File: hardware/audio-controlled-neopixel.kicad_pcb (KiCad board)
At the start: 2 copper layers, 96 x 56 mm, 63 parts, among them J1 AudioJack3_Ground, J2 AudioJack3_Ground, J3 KF2EDGK, J4 KF2EDGK, J5 KF2EDGK, J6 Conn_01x01_Female, J7 Conn_01x01_Female, J8 Conn_01x01_Female, J9 Conn_01x01_Female, SW1 SW_SPST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

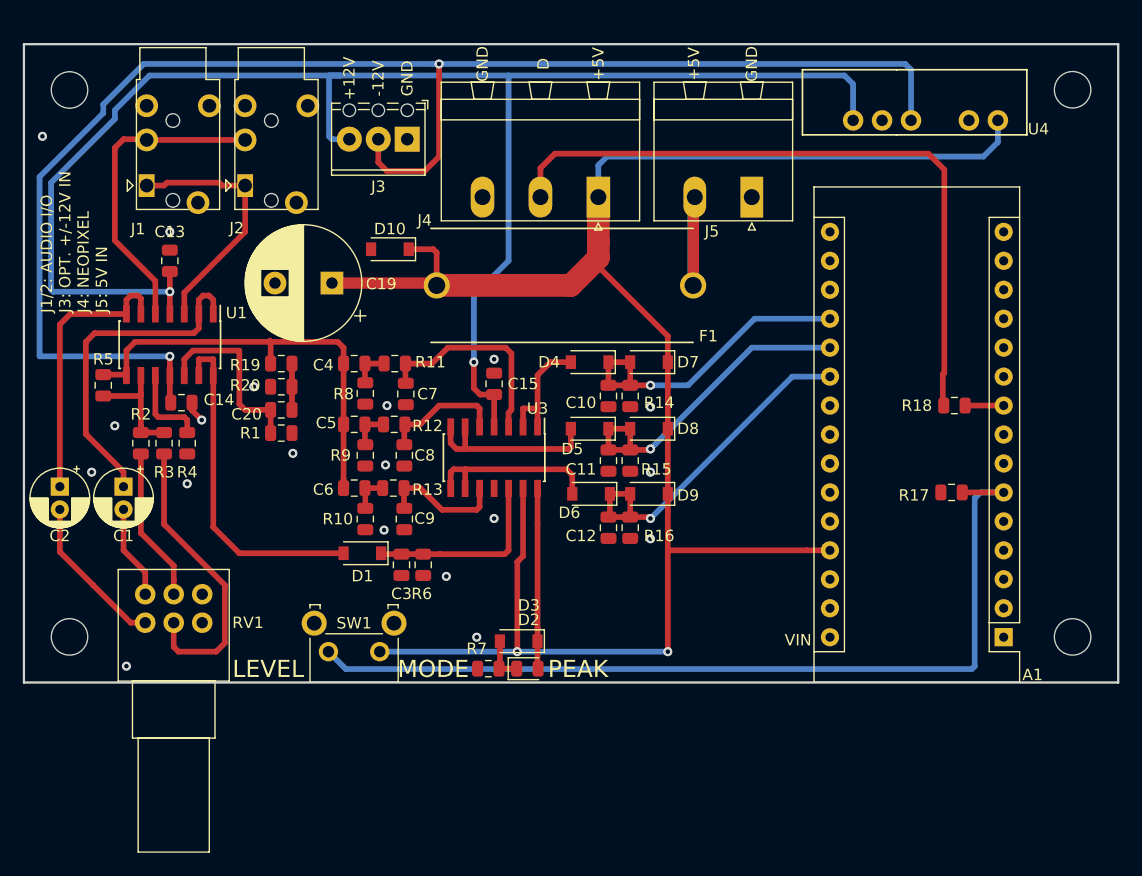
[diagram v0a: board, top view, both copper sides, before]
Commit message: updated some footprints and symbols
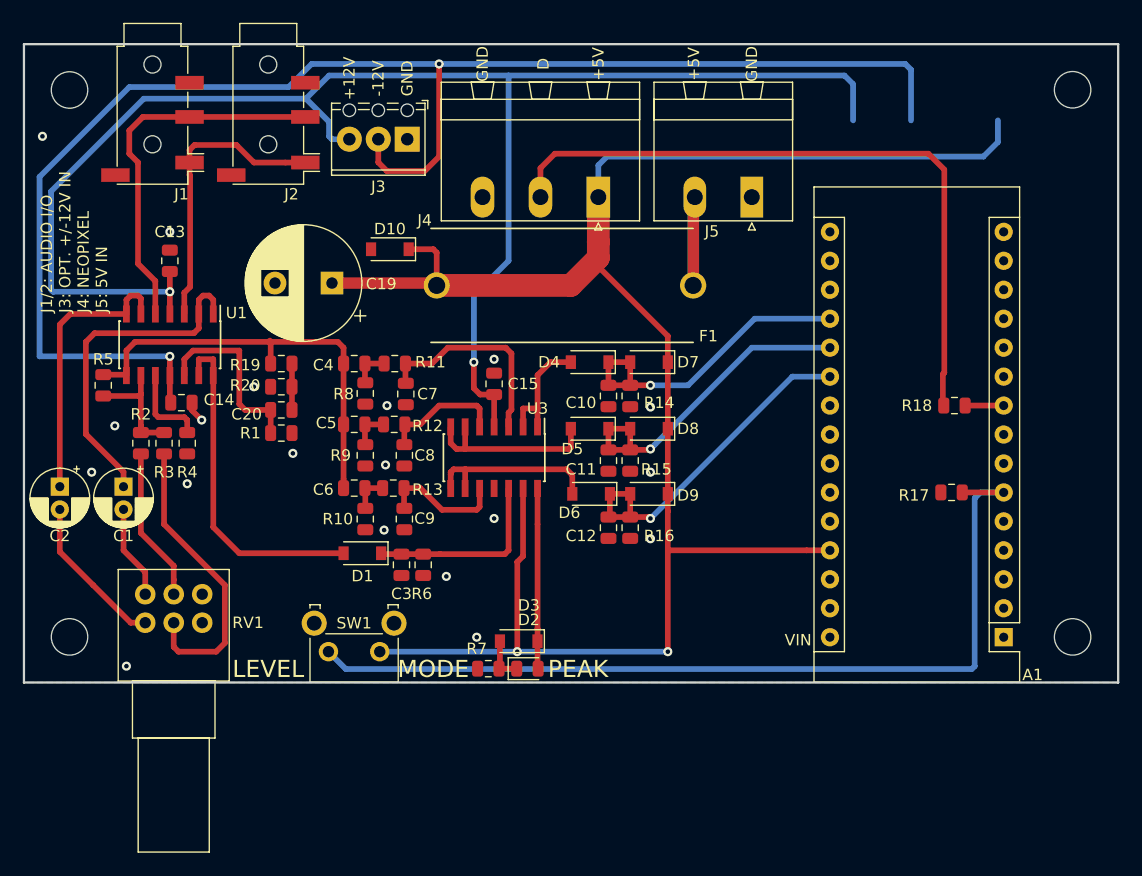
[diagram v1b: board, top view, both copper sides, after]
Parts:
- removed U4: TMA0512D, Footprints:TMAxxxxD
- J1, J2: value AudioJack3_Ground -> AudioJack4; footprint Footprints:Jack_3.5mm_PJ320E_Horizontal -> Connector_Audio:Jack_3.5mm_PJ320D_Horizontal
- R19: value 100K -> 10K
- moved J2 6.19 mm to (59.4, 35.6), turned to 270 degrees
- moved J1 5.86 mm to (49.3, 35.6), turned to 270 degrees
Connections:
- U1 pad 3: /Input_L -> /Input_R
- U1 pad 5: /Input_R -> /Input_L
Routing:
- net /Input_L: track 22.3 -> 33.0 mm
- net +12V: track 143.6 -> 140.5 mm
- net /Input_R: track 27.8 -> 25.6 mm
- net (no net): track 0.51 -> 0.00 mm

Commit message: PCB bugfix, rearranged code
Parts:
- added U2: TMA0512D, custom:TMA-0512D, F.Cu at (125.7, 29.7)
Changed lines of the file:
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@@
     (tracks 322)
     (zones 0)
-    (modules 62)
+    (modules 63)
     (nets 66)
   )
@@
   )
   (setup
-    (last_trace_width 0.5)
+    (last_trace_width 0.25)
     (user_trace_width 0.5)
     (user_trace_width 1)
@@
     (add_net "Net-(R4-Pad1)")
   )
+  (module custom:TMA-0512D (layer F.Cu)
+    (at 125.73 29.718 180)
+    (descr TMA-0512D)
+    (tags Transformer)
+    (fp_text reference U2 (at 9.442 -3.40167 180) (layer F.SilkS)
+      (effects (font (size 1.27 1.27) (thickness 0.254)))
+    )
+    (fp_text value TMA0512D (at 9.442 -3.40167 180) (layer F.SilkS) hide
+      (effects (font (size 1.27 1.27) (thickness 0.254)))
+    )
+    (fp_line (start 0 0) (end 0 -7.1) (layer F.SilkS) (width 0.15))
+    (fp_line (start 0 -7.1) (end 19.5 -7.1) (layer F.SilkS) (width 0.15))
+    (fp_line (start 19.5 -7.1) (end 19.5 0) (layer F.SilkS) (width 0.15))
+    (fp_line (start 19.5 0) (end 0 0) (layer F.SilkS) (width 0.15))
+    (fp_circle (center 2.646665 -7.95033) (end 2.3726 -7.95033) (layer F.SilkS) (width 0.254))
+    (pad 1 thru_hole circle (at 2.4 -5.95 270) (size 1.33 1.33) (drill 0.83) (layers *.Cu *.Mask)
+      (net 7 +5V))
+    (pad 2 thru_hole circle (at 4.94 -5.95 270) (size 1.33 1.33) (drill 0.83) (layers *.Cu *.Mask)
+      (net 1 GND))
+    (pad 4 thru_hole circle (at 10.02 -5.95 270) (size 1.33 1.33) (drill 0.83) (layers *.Cu *.Mask)
+      (net 21 -12V))
+    (pad 5 thru_hole circle (at 12.56 -5.95 270) (size 1.33 1.33) (drill 0.83) (layers *.Cu *.Mask)
+      (net 1 GND))
+    (pad 6 thru_hole circle (at 15.1 -5.95 270) (size 1.33 1.33) (drill 0.83) (layers *.Cu *.Mask)
+      (net 22 +12V))
+  )
   (module Connector_Audio:Jack_3.5mm_PJ320D_Horizontal (layer F.Cu)
     (at 49.276 35.56 270)
@@
   (segment (start 75.438 64.008) (end 75.946 64.516) (width 0.5) (layer F.Cu) (net 25))
   (segment (start 123.952 60.706) (end 120.5715 60.706) (width 0.5) (layer F.Cu) (net 36))
-  (segment (start 49.53 49.784) (end 49.53 52.672) (width 0.5) (layer F.Cu) (net 49))
   (segment (start 52.07 50.8) (end 52.07 52.672) (width 0.5) (layer F.Cu) (net 48))
   (segment (start 52.526 40.485) (end 52.578 40.537) (width 0.5) (layer F.Cu) (net 48))
@@
   (segment (start 56.642 37.846) (end 58.181 39.385) (width 0.5) (layer F.Cu) (net 48))
   (segment (start 52.526 38.285) (end 52.965 37.846) (width 0.5) (layer F.Cu) (net 48))
+  (segment (start 49.53 49.784) (end 49.53 52.672) (width 0.5) (layer F.Cu) (net 49))
   (segment (start 52.526 35.385) (end 62.686 35.385) (width 0.5) (layer F.Cu) (net 49))
   (segment (start 52.526 35.385) (end 48.435 35.385) (width 0.5) (layer F.Cu) (net 49))

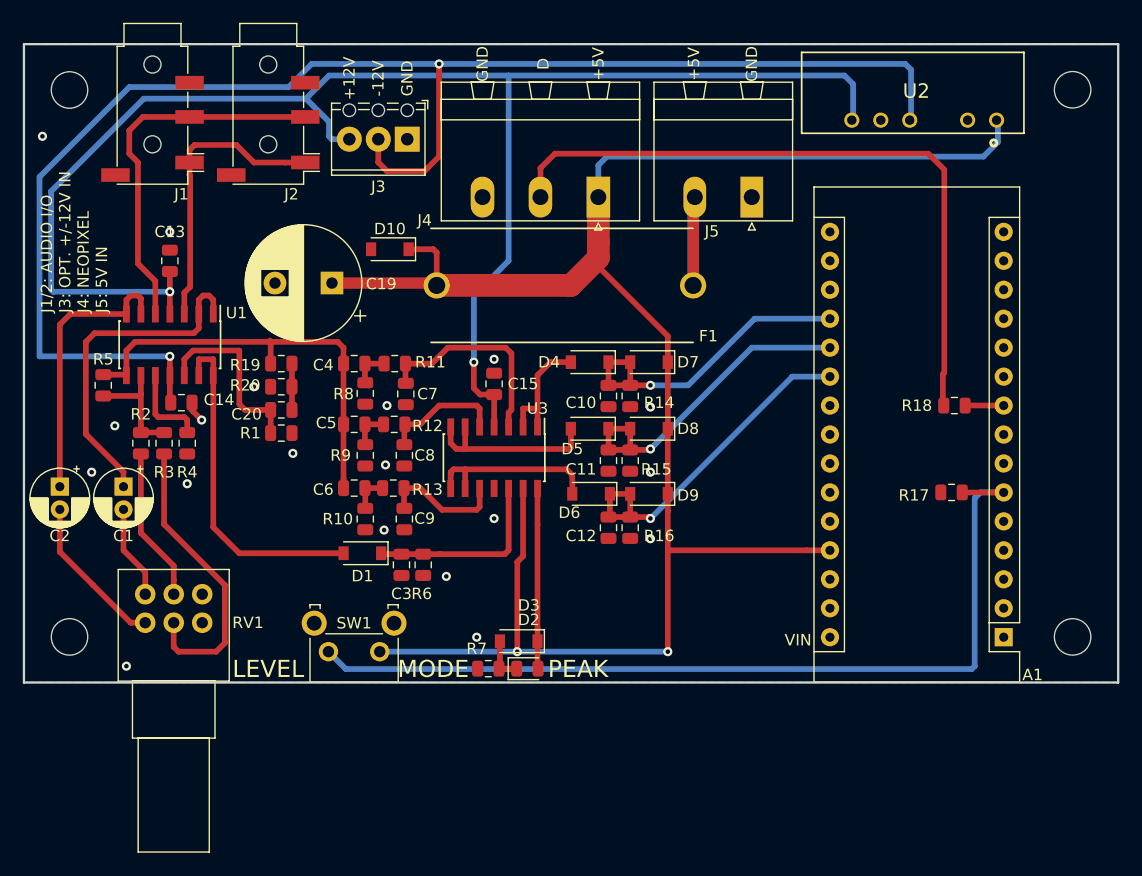
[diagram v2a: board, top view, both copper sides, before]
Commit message: added attenuators to balance frequency response
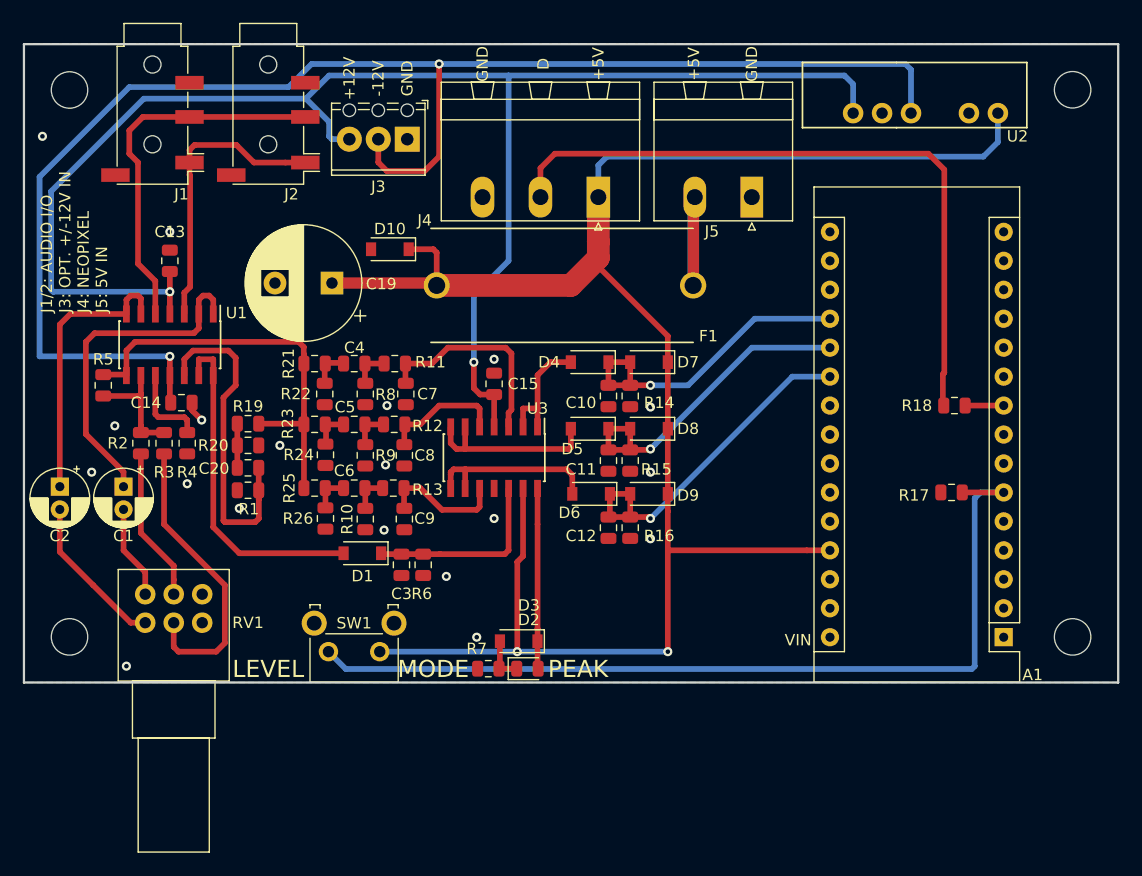
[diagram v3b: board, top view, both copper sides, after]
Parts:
- added R21: 100K, Resistor_SMD:R_0805_2012Metric, F.Cu at (63.5, 57.0)
- added R22: 250K, Resistor_SMD:R_0805_2012Metric, F.Cu at (64.4, 59.7)
- added R23: 100K, Resistor_SMD:R_0805_2012Metric, F.Cu at (63.5, 62.4)
- added R24: 169K, Resistor_SMD:R_0805_2012Metric, F.Cu at (64.5, 65.0)
- added R25: 0R, Resistor_SMD:R_0805_2012Metric, F.Cu at (63.5, 67.9)
- added R26: NF, Resistor_SMD:R_0805_2012Metric, F.Cu at (64.5, 70.6)
- R19: value 10K -> 100K
- U2: footprint custom:TMA-0512D -> Footprints:TMAxxxxD
- moved R19 6.03 mm to (57.7, 62.3)
- moved R20 5.92 mm to (57.7, 64.2), turned to 180 degrees
- moved C20 5.86 mm to (57.7, 66.2), turned to 180 degrees
- moved R1 5.80 mm to (57.7, 68.1), turned to 180 degrees
- moved U2 0.92 mm to (126.0, 30.6)
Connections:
- C4 pad 2: /Buf_input -> Net-(C4-Pad2)
- C5 pad 2: /Buf_input -> Net-(C5-Pad2)
- C6 pad 2: /Buf_input -> Net-(C6-Pad2)
- R19 pad 1: /Buf_input -> Net-(C20-Pad2)
- R19 pad 2: Net-(C20-Pad2) -> /Buf_input
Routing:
- net Net-(C20-Pad1): track 16.3 -> 29.0 mm
- net Net-(C4-Pad2): track 0.00 -> 3.67 mm
- net Net-(C6-Pad2): track 0.00 -> 3.34 mm
- net Net-(C5-Pad2): track 0.00 -> 3.29 mm
- net /Buf_input: track 38.3 -> 36.7 mm
- net -12V: track 132.6 -> 131.9 mm
- net +12V: track 140.5 -> 139.8 mm

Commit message: removed analogue clipping hardware to prepare for transisiton to software solution (not implemented)
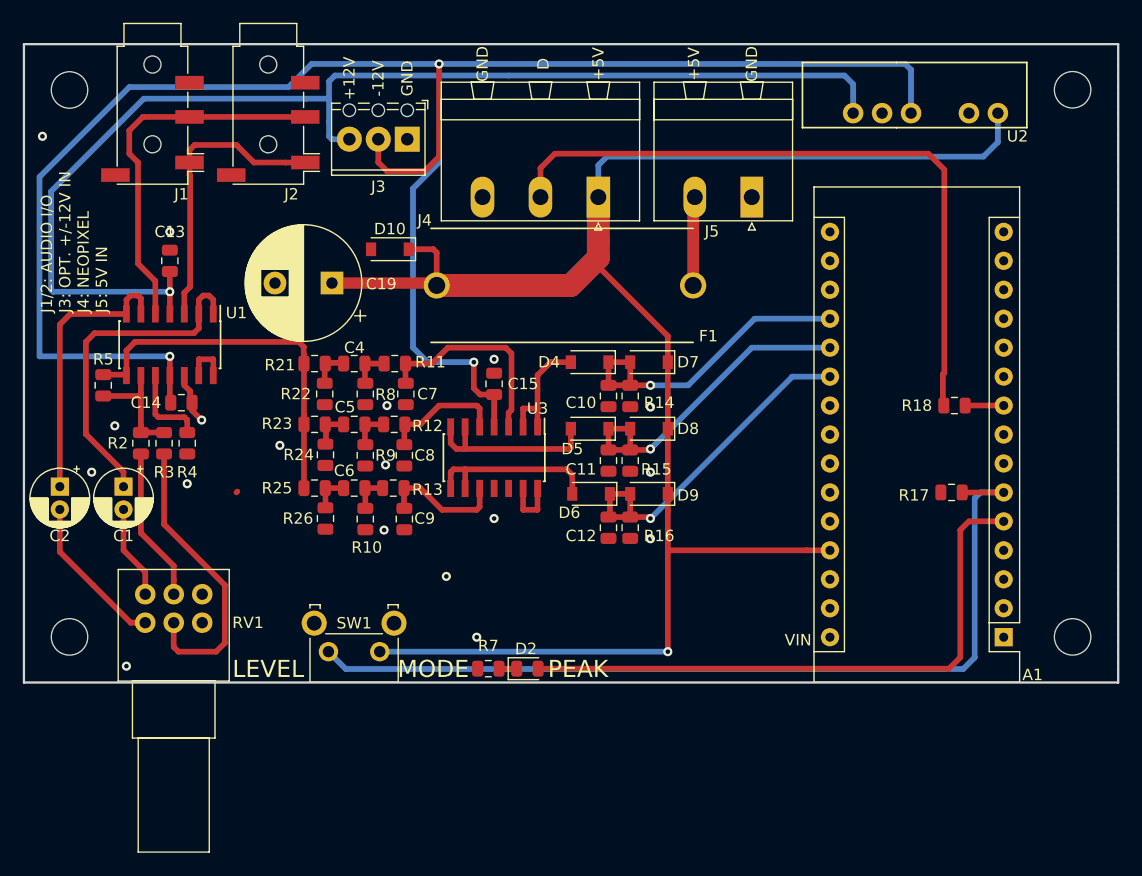
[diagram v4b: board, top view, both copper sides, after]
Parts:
- removed C20, C3: 100n, Capacitor_SMD:C_0805_2012Metric
- removed D1: 1N4148, Diode_SMD:D_SOD-123
- removed D3: 1N5819, Diode_SMD:D_SOD-123
- removed R1, R19, R20: 100K, Resistor_SMD:R_0805_2012Metric
- removed R6: 1M, Resistor_SMD:R_0805_2012Metric
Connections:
- A1 pad 5: Net-(A1-Pad5) -> /Clipping
- D2 pad 2: Net-(D2-Pad2) -> /Clipping
- U1 pad 12: Net-(C20-Pad1) -> GND
- U3 pad 12: Net-(C3-Pad1) -> GND
- U3 pad 13: +5V -> Net-(U3-Pad13)
- U3 pad 14: Net-(D2-Pad2) -> Net-(U3-Pad13)
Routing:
- net /Clipping: track 0.00 -> 52.7 mm
- net Net-(C20-Pad1): track 29.0 -> 0.00 mm
- net Net-(U1-Pad13): track 29.8 -> 4.13 mm
- net Net-(C3-Pad1): track 16.8 -> 0.00 mm
- net Net-(D2-Pad2): track 15.8 -> 0.00 mm
- net +5V: track 167.1 -> 173.0 mm, vias 2 -> 1
- net Net-(U3-Pad13): track 0.00 -> 5.01 mm
- net +12V: track 139.8 -> 144.2 mm
- net /Buf_input: track 36.7 -> 32.7 mm
- net Net-(C20-Pad2): track 3.87 -> 0.00 mm
- net GND: track 2.78 -> 5.45 mm, vias 19 -> 18
- net Net-(D2-Pad1): track 4.00 -> 1.67 mm

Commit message: tag for prototype production
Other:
- board text added: "Audio Controlled Neopixel Driver Designed by Joe Earlam Rev: p2"
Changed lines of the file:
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@@
-(kicad_pcb (version 20171130) (host pcbnew "(5.0.2)-1")
+(kicad_pcb (version 20171130) (host pcbnew 5.0.2-bee76a0~70~ubuntu16.04.1)
   (general
     (thickness 1.6)
-    (drawings 17)
+    (drawings 18)
     (tracks 319)
     (zones 0)
@@
   )
   (setup
-    (last_trace_width 0.5)
+    (last_trace_width 0.25)
     (user_trace_width 0.5)
     (user_trace_width 1)
@@
       (drillshape 0)
       (scaleselection 1)
-      (outputdirectory "Gerbers/"))
+      (outputdirectory "../../../../../gerbers/neopixel/"))
   )
   (net 0 "")
@@
     (tags diode)
     (attr smd)
-    (fp_text reference D2 (at -0.127 -1.746) (layer F.SilkS)
+    (fp_text reference D2 (at -1.905 -1.746) (layer F.SilkS)
       (effects (font (size 1 1) (thickness 0.15)))
     )
@@
     (tags resistor)
     (attr smd)
-    (fp_text reference R7 (at 0 2 180) (layer F.SilkS)
+    (fp_text reference R7 (at 0.762 1.746 180) (layer F.SilkS)
       (effects (font (size 1 1) (thickness 0.15)))
     )
@@
     )
   )
+  (gr_text "Audio Controlled\nNeopixel Driver\nDesigned by Joe Earlam\nRev: p2" (at 81.28 77.724) (layer F.SilkS)
+    (effects (font (size 1.4 1.4) (thickness 0.3)) (justify left))
+  )
   (gr_text VIN (at 105.918 81.28) (layer F.SilkS)
     (effects (font (size 1 1) (thickness 0.2)))
@@
   (gr_line (start 38 29) (end 134 29) (layer Edge.Cuts) (width 0.2))
   (gr_line (start 38 85) (end 38 29) (layer Edge.Cuts) (width 0.2))
-  (segment (start 53.34 56.642) (end 53.34 58.072) (width 0.5) (layer F.Cu) (net 65))
-  (segment (start 54.61 58.072) (end 54.61 56.642) (width 0.5) (layer F.Cu) (net 65))
-  (segment (start 54.61 56.642) (end 53.34 56.642) (width 0.5) (layer F.Cu) (net 65))
   (via (at 69.85 60.706) (size 0.8) (drill 0.4) (layers F.Cu B.Cu) (net 1))
   (via (at 69.723 65.913) (size 0.8) (drill 0.4) (layers F.Cu B.Cu) (net 1))
@@
   (segment (start 81.788 67.978) (end 81.788 69.85) (width 0.5) (layer F.Cu) (net 64))
   (segment (start 81.788 69.85) (end 83.058 69.85) (width 0.5) (layer F.Cu) (net 64))
+  (segment (start 53.34 56.642) (end 53.34 58.072) (width 0.5) (layer F.Cu) (net 65))
+  (segment (start 54.61 58.072) (end 54.61 56.642) (width 0.5) (layer F.Cu) (net 65))
+  (segment (start 54.61 56.642) (end 53.34 56.642) (width 0.5) (layer F.Cu) (net 65))
   (zone (net 1) (net_name GND) (layer F.Cu) (hatch edge 0.508)
     (connect_pads (clearance 0.508))
